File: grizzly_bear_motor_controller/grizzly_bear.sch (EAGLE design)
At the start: 54 parts, among them Q1 PH7030L, Q2 PH7030L, Q3 PH7030L, Q4 PH7030L, Q5 FDD4141TO252, U1 A4940, U2 ATMEGA32U4-AU, U3 ACS714, U4 UA78L00, Y1 16MHz

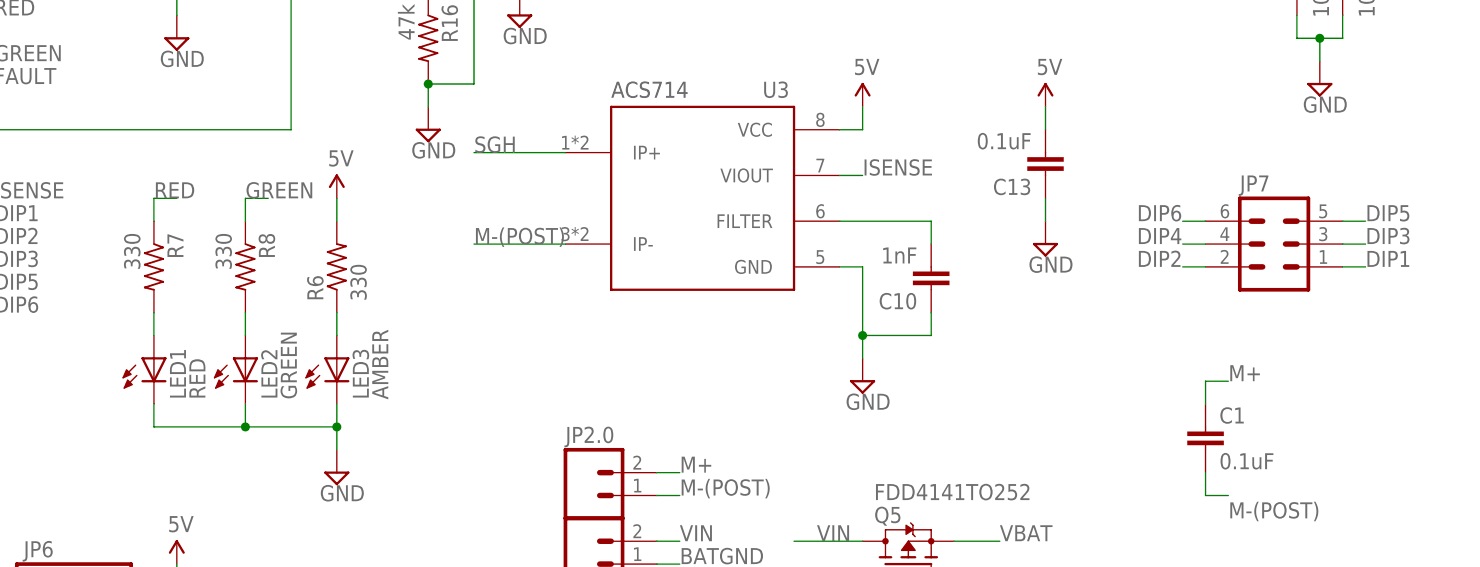
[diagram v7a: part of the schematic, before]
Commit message: Rearrange silkscreen and update revision to rev. B
Change-Id: If26ab9740f1918a3d609a33e18ff4d090503f5e5
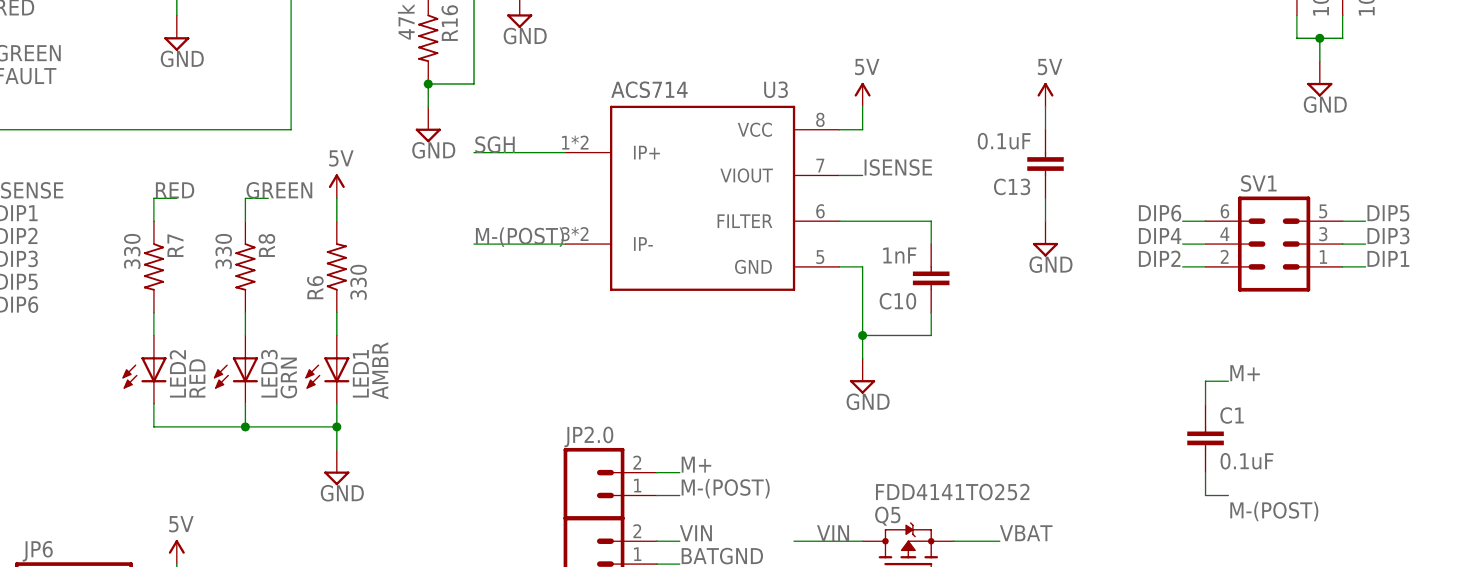
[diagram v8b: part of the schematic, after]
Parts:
- removed JP7: (no value), con-lstb:MA03-2
- added SV1: (no value), pie:MA03-2
- LED1: value RED -> AMBR
- LED2: value GREEN -> RED
- LED3: value AMBER -> GRN
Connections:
- net DIP1: now also SV1.1; no longer JP7.1
- net DIP2: now also SV1.2; no longer JP7.2
- net DIP3: now also SV1.3; no longer JP7.3
- net DIP4: now also SV1.4; no longer JP7.4
- net DIP5: now also SV1.5; no longer JP7.5
- net DIP6: now also SV1.6; no longer JP7.6
- net N$23: now also LED2.A; no longer LED1.A
- net N$25: now also LED1.A; no longer LED3.A
- net N$5: now also LED3.A; no longer LED2.A
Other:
- moved on the sheet: LED1, LED2, LED3
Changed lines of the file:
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@@
 <part name="JP2.0" library="SparkFun-Connectors" deviceset="M02" device="PTH4"/>
 <part name="JP1.0" library="SparkFun-Connectors" deviceset="M02" device="PTH4"/>
-<part name="LED1" library="SparkFun-LED" deviceset="LED" device="1206" value="RED"/>
-<part name="LED2" library="SparkFun-LED" deviceset="LED" device="1206" value="GREEN"/>
+<part name="LED2" library="SparkFun-LED" deviceset="LED" device="1206" value="RED"/>
+<part name="LED3" library="SparkFun-LED" deviceset="LED" device="1206" value="GRN"/>
 <part name="R8" library="resistor" deviceset="R-US_" device="R0603" value="330"/>
 <part name="R7" library="resistor" deviceset="R-US_" device="R0603" value="330"/>
-<part name="LED3" library="SparkFun-LED" deviceset="LED" device="1206" value="AMBER"/>
+<part name="LED1" library="SparkFun-LED" deviceset="LED" device="1206" value="AMBR"/>
 <part name="R6" library="resistor" deviceset="R-US_" device="R0603" value="330"/>
 <part name="U$13" library="SparkFun-Aesthetics" deviceset="5V" device=""/>
@@
 <part name="SUPPLY1" library="supply2" deviceset="GND" device=""/>
 <part name="U4" library="pie" deviceset="UA78L00" device=""/>
-<part name="JP7" library="con-lstb" deviceset="MA03-2" device=""/>
 <part name="U$14" library="SparkFun-Aesthetics" deviceset="5V" device=""/>
 <part name="C100" library="pie" deviceset="CAP_POL" device="G" value="470uF"/>
 <part name="Y1" library="pie" deviceset="CRYSTAL" device="HC49US" value="16MHz"/>
+<part name="SV1" library="pie" deviceset="MA03-2" device=""/>
 </parts>
 <sheets>
@@
 <attribute name="NAME" x="55.88" y="-22.86" size="1.778" layer="95"/>
 </instance>
-<instance part="LED1" gate="G$1" x="10.16" y="5.08"/>
-<instance part="LED2" gate="G$1" x="20.32" y="5.08"/>
+<instance part="LED2" gate="G$1" x="10.16" y="5.08"/>
+<instance part="LED3" gate="G$1" x="20.32" y="5.08"/>
 <instance part="R8" gate="G$1" x="20.32" y="15.24" rot="R270"/>
 <instance part="R7" gate="G$1" x="10.16" y="15.24" rot="R270"/>
-<instance part="LED3" gate="G$1" x="30.48" y="5.08"/>
+<instance part="LED1" gate="G$1" x="30.48" y="5.08"/>
 <instance part="R6" gate="G$1" x="30.48" y="15.24" rot="R90"/>
 <instance part="U$13" gate="G$1" x="30.48" y="22.86"/>
@@
 <instance part="SUPPLY1" gate="GND" x="40.64" y="30.48"/>
 <instance part="U4" gate="G$1" x="-43.18" y="121.92"/>
-<instance part="JP7" gate="1" x="134.62" y="17.78"/>
 <instance part="U$14" gate="G$1" x="-25.4" y="127"/>
 <instance part="C100" gate="G$1" x="124.46" y="114.3"/>
@@
 <attribute name="VALUE" x="-76.2" y="45.72" size="1.778" layer="96" rot="R90"/>
 </instance>
+<instance part="SV1" gate="1" x="134.62" y="17.78"/>
 </instances>
 <busses>
@@
 </segment>
 <segment>
-<pinref part="LED3" gate="G$1" pin="C"/>
+<pinref part="LED1" gate="G$1" pin="C"/>
 <pinref part="SUPPLY14" gate="GND" pin="GND"/>
 <wire x1="30.48" y1="-5.08" x2="30.48" y2="-2.54" width="0.1524" layer="91"/>
-<pinref part="LED2" gate="G$1" pin="C"/>
+<pinref part="LED3" gate="G$1" pin="C"/>
 <wire x1="30.48" y1="-2.54" x2="30.48" y2="0" width="0.1524" layer="91"/>
 <wire x1="20.32" y1="0" x2="20.32" y2="-2.54" width="0.1524" layer="91"/>
 <wire x1="20.32" y1="-2.54" x2="30.48" y2="-2.54" width="0.1524" layer="91"/>
-<pinref part="LED1" gate="G$1" pin="C"/>
+<pinref part="LED2" gate="G$1" pin="C"/>
 <wire x1="10.16" y1="0" x2="10.16" y2="-2.54" width="0.1524" layer="91"/>
 <wire x1="10.16" y1="-2.54" x2="20.32" y2="-2.54" width="0.1524" layer="91"/>
@@
 <segment>
 <pinref part="R8" gate="G$1" pin="2"/>
+<pinref part="LED3" gate="G$1" pin="A"/>
+<wire x1="20.32" y1="10.16" x2="20.32" y2="7.62" width="0.1524" layer="91"/>
+</segment>
+</net>
+<net name="N$23" class="0">
+<segment>
 <pinref part="LED2" gate="G$1" pin="A"/>
-<wire x1="20.32" y1="10.16" x2="20.32" y2="7.62" width="0.1524" layer="91"/>
-</segment>
-</net>
-<net name="N$23" class="0">
-<segment>
-<pinref part="LED1" gate="G$1" pin="A"/>
 <pinref part="R7" gate="G$1" pin="2"/>
 <wire x1="10.16" y1="7.62" x2="10.16" y2="10.16" width="0.1524" layer="91"/>
@@
 <segment>
 <pinref part="R6" gate="G$1" pin="1"/>
-<pinref part="LED3" gate="G$1" pin="A"/>
+<pinref part="LED1" gate="G$1" pin="A"/>
 <wire x1="30.48" y1="7.62" x2="30.48" y2="10.16" width="0.1524" layer="91"/>
 </segment>
@@
 <net name="DIP1" class="0">
 <segment>
-<pinref part="JP7" gate="1" pin="1"/>
-<wire x1="142.24" y1="15.24" x2="144.78" y2="15.24" width="0.1524" layer="91"/>
 <label x="144.78" y="15.24" size="1.778" layer="95"/>
+<pinref part="SV1" gate="1" pin="1"/>
+<wire x1="144.78" y1="15.24" x2="142.24" y2="15.24" width="0.1524" layer="91"/>
 </segment>
 <segment>
@@
 <net name="DIP3" class="0">
 <segment>
-<pinref part="JP7" gate="1" pin="3"/>
-<wire x1="142.24" y1="17.78" x2="144.78" y2="17.78" width="0.1524" layer="91"/>
 <label x="144.78" y="17.78" size="1.778" layer="95"/>
+<pinref part="SV1" gate="1" pin="3"/>
+<wire x1="144.78" y1="17.78" x2="142.24" y2="17.78" width="0.1524" layer="91"/>
 </segment>
 <segment>
@@
 <net name="DIP5" class="0">
 <segment>
-<pinref part="JP7" gate="1" pin="5"/>
 <wire x1="142.24" y1="20.32" x2="144.78" y2="20.32" width="0.1524" layer="91"/>
 <label x="144.78" y="20.32" size="1.778" layer="95"/>
+<pinref part="SV1" gate="1" pin="5"/>
 </segment>
 <segment>
@@
 <net name="DIP6" class="0">
 <segment>
-<pinref part="JP7" gate="1" pin="6"/>
 <wire x1="127" y1="20.32" x2="124.46" y2="20.32" width="0.1524" layer="91"/>
 <label x="119.38" y="20.32" size="1.778" layer="95"/>
+<pinref part="SV1" gate="1" pin="6"/>
 </segment>
 <segment>
@@
 <net name="DIP4" class="0">
 <segment>
-<pinref part="JP7" gate="1" pin="4"/>
 <wire x1="127" y1="17.78" x2="124.46" y2="17.78" width="0.1524" layer="91"/>
 <label x="119.38" y="17.78" size="1.778" layer="95"/>
+<pinref part="SV1" gate="1" pin="4"/>
 </segment>
 <segment>
@@
 <net name="DIP2" class="0">
 <segment>
-<pinref part="JP7" gate="1" pin="2"/>
 <wire x1="127" y1="15.24" x2="124.46" y2="15.24" width="0.1524" layer="91"/>
 <label x="119.38" y="15.24" size="1.778" layer="95"/>
-</segment>
-<segment>
+<pinref part="SV1" gate="1" pin="2"/>
+</segment>
+<segment>
